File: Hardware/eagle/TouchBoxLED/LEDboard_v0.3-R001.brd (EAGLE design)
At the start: 160 x 100 mm, 11 parts, among them X2 22-23-2021

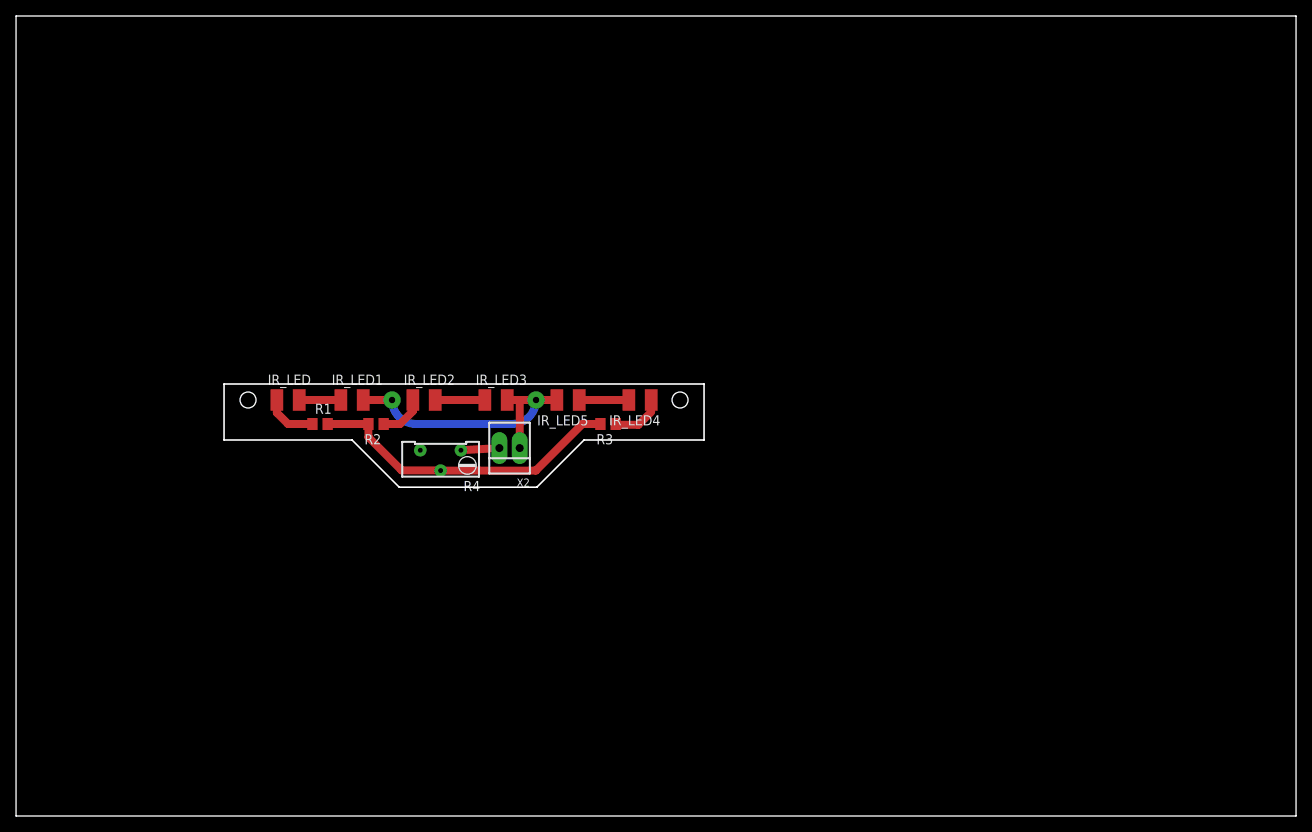
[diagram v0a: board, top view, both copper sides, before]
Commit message: new PressureBase design restructuring of design folder
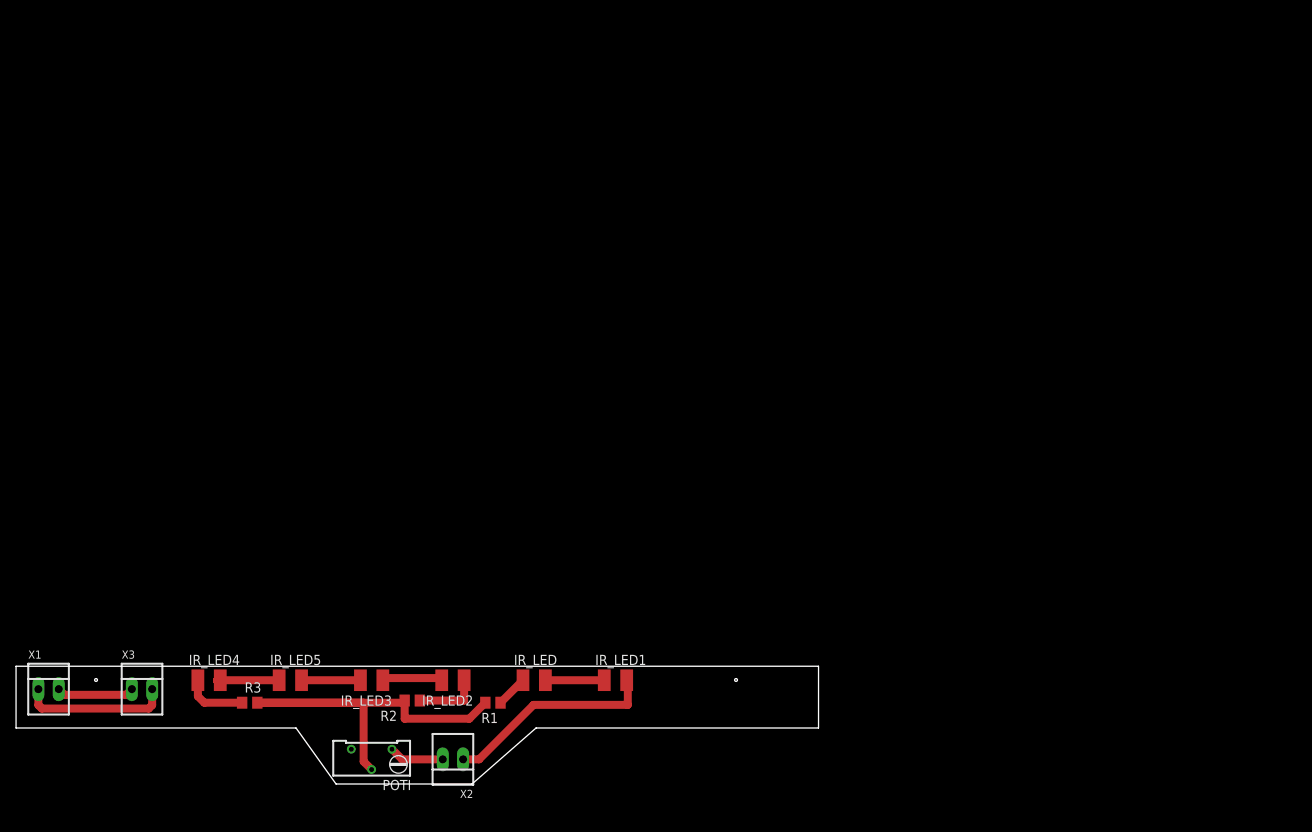
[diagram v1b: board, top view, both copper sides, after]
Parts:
- removed R4: (no value), rcl:RTRIM64Y
- added POTI: 500, rcl:RTRIM64Y
- added X1, X3: 22-23-2021, con-molex:22-23-2021
- R1, R2, R3: value (none) -> 10
- moved IR_LED4 64.3 mm to (24.1, 17.0), turned to 0 degrees
- moved R3 56.7 mm to (29.2, 14.2), turned to 0 degrees
- moved IR_LED5 49.3 mm to (34.3, 17.0), turned to 0 degrees
- moved IR_LED1 48.1 mm to (74.9, 17.0)
- moved IR_LED 46.6 mm to (64.8, 17.0)
- moved R1 41.0 mm to (59.6, 14.2), turned to 180 degrees
- moved X2 39.5 mm to (54.6, 7.08)
- moved IR_LED3 38.3 mm to (44.5, 17.0), turned to 180 degrees
- moved IR_LED2 35.2 mm to (54.6, 17.0), turned to 180 degrees
- moved R2 34.9 mm to (49.5, 14.4)
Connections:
- new net N$10: X1.2, X3.1
- new net N$11: X1.1, X3.2
- net N$7: now also POTI.2; no longer R4.2
- net N$9: now also POTI.1; no longer R4.1
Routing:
- net N$11: track 0.00 -> 18.6 mm
- net N$7: track 39.9 -> 53.8 mm
- net N$10: track 0.00 -> 9.74 mm
- net N$2: track 6.63 -> 3.97 mm
- net N$4: track 5.71 -> 8.07 mm
- net N$8: track 36.3 -> 34.0 mm, vias 2 -> 0
- net N$1: track 5.20 -> 7.36 mm
- net N$9: track 4.82 -> 6.88 mm
- net N$5: track 6.20 -> 8.20 mm
- net N$3: track 6.20 -> 7.58 mm
- net N$6: track 6.65 -> 7.87 mm
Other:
- board size 160 x 100 mm -> 100.3 x 14.7 mm
